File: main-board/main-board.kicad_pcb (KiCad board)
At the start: 2 copper layers, 101 x 101 mm, 18 parts, among them J1 C10418, J2 FH12-24S-0.5SH(55), U1 ESP-32s, U2 HT7333-A, U3 CH340E

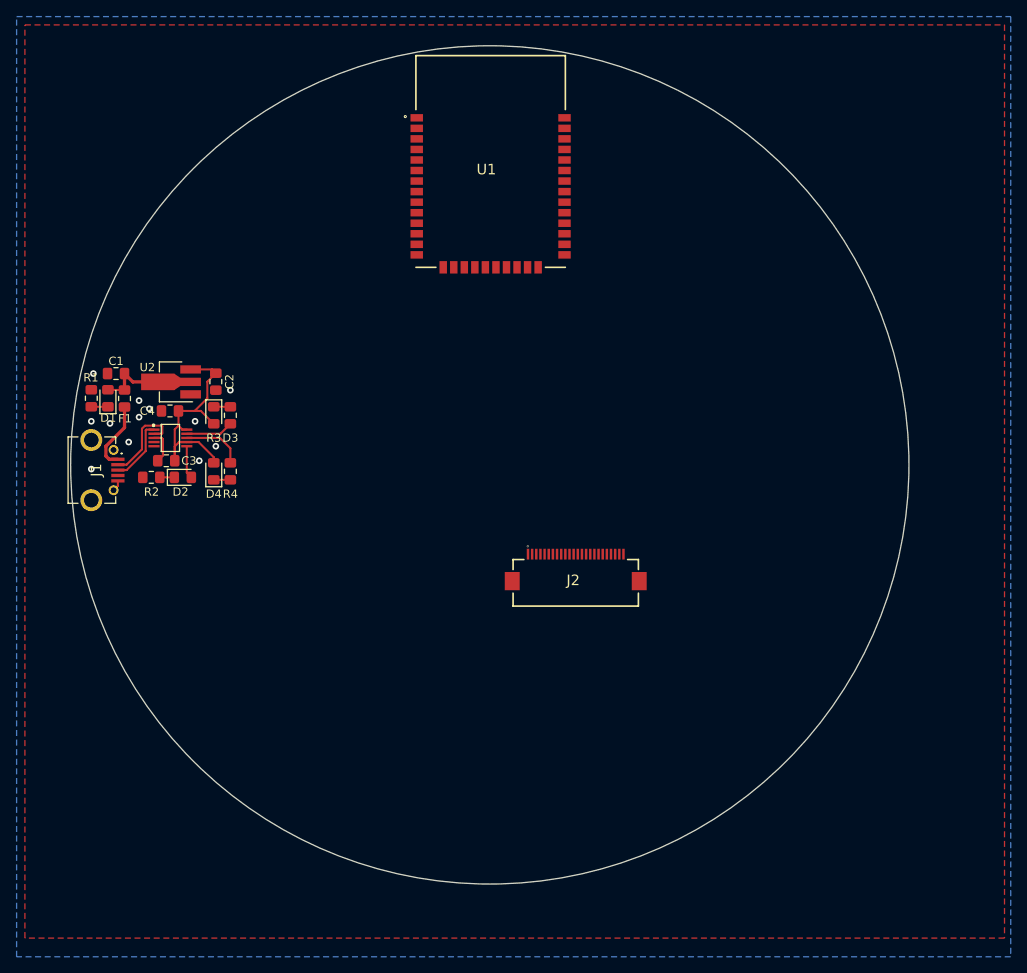
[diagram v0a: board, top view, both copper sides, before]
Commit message: battery holder
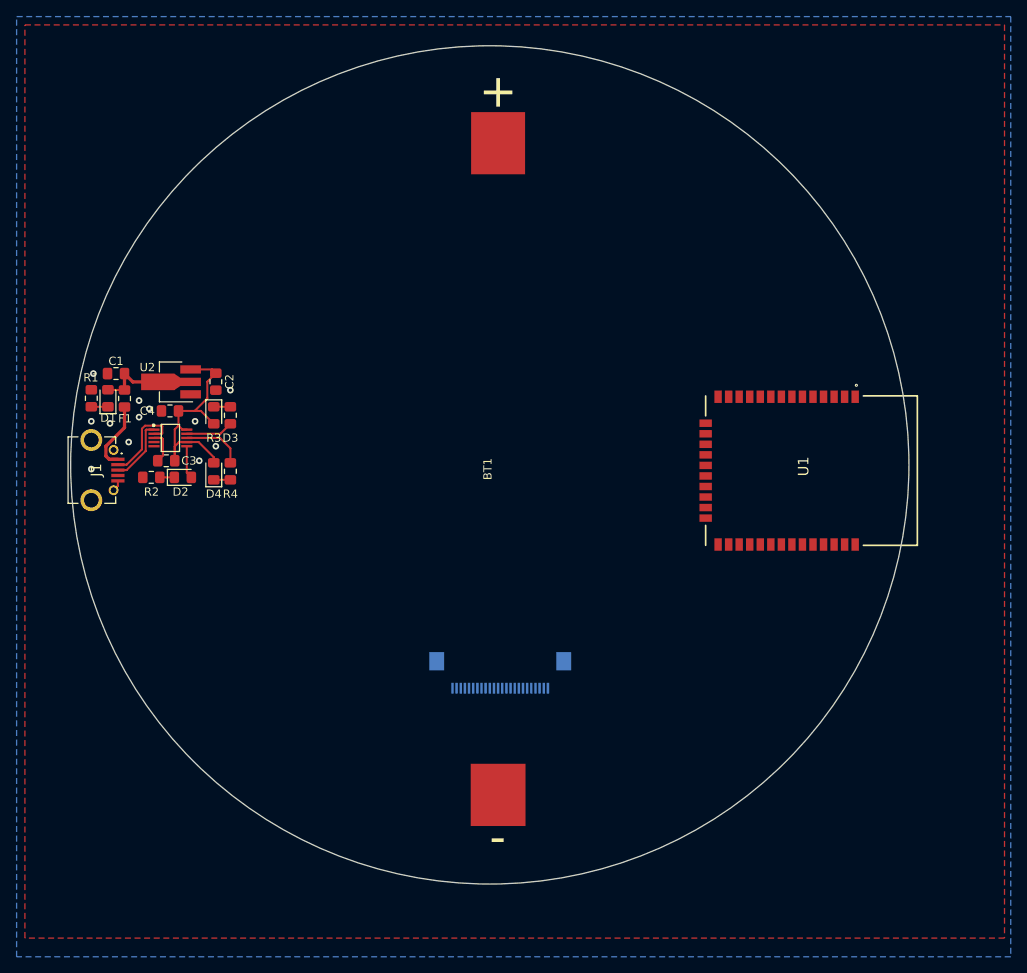
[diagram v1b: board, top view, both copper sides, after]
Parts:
- added BT1: Battery_Holder, water-lib:Battery Holder SMD, F.Cu at (146.0, 90.5)
- J2: moved to B.Cu
- moved U1 35.6 mm to (171.0, 90.7), turned to 270 degrees
- moved J2 17.4 mm to (146.2, 116.2)

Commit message: battery protection + buckboost
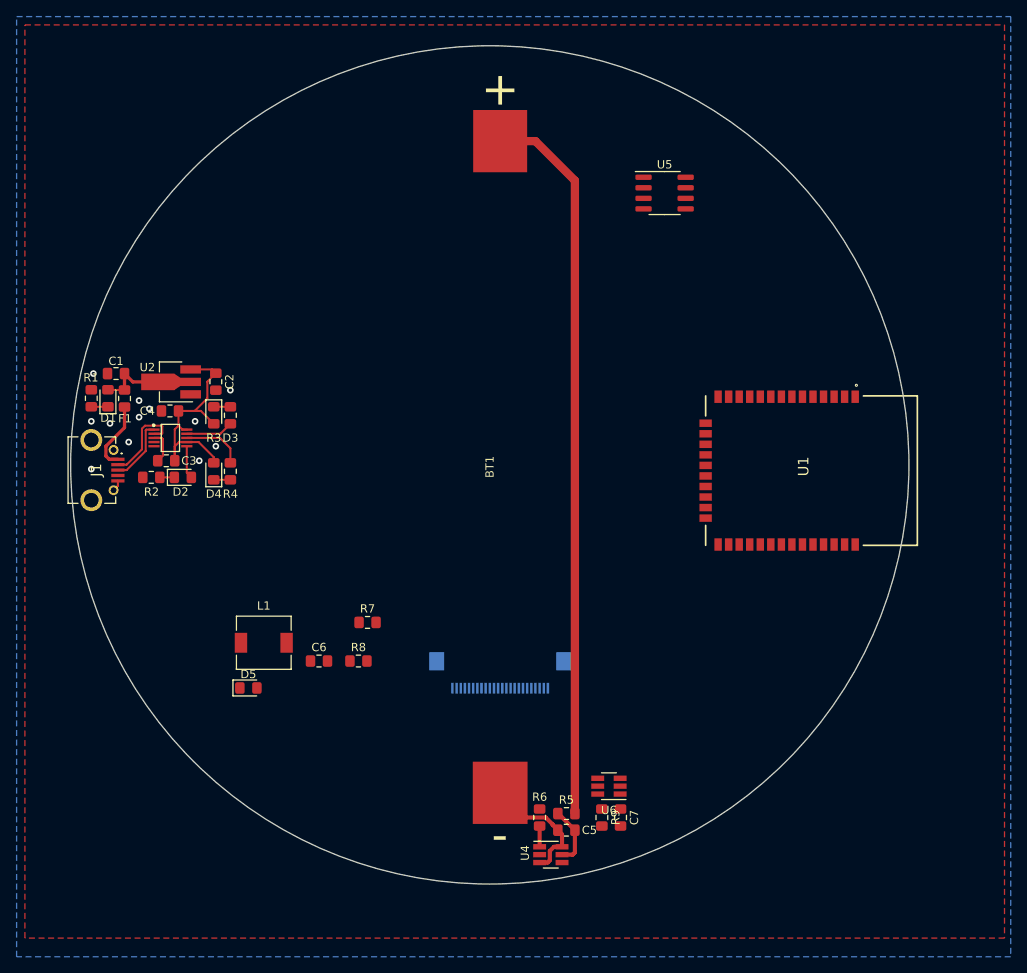
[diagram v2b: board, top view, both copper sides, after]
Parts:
- added C5: 0.1uF, Capacitor_SMD:C_0805_2012Metric_Pad1.15x1.40mm_HandSolder, F.Cu at (154.2, 134.0)
- added C6: 22uF, Capacitor_SMD:C_0805_2012Metric_Pad1.15x1.40mm_HandSolder, F.Cu at (124.4, 113.6)
- added C7: 22uF, Capacitor_SMD:C_0805_2012Metric_Pad1.15x1.40mm_HandSolder, F.Cu at (160.8, 132.5)
- added D5: D_Schottky, Diode_SMD:D_0805_2012Metric_Pad1.15x1.40mm_HandSolder, F.Cu at (115.9, 116.9)
- added L1: 22uH, Inductor_SMD:L_6.3x6.3_H3, F.Cu at (117.8, 111.4)
- added R5: 100, Resistor_SMD:R_0805_2012Metric_Pad1.15x1.40mm_HandSolder, F.Cu at (154.2, 132.0)
- added R6: 1k, Resistor_SMD:R_0805_2012Metric_Pad1.15x1.40mm_HandSolder, F.Cu at (151.0, 132.5)
- added R7: 10k, Resistor_SMD:R_0805_2012Metric_Pad1.15x1.40mm_HandSolder, F.Cu at (130.3, 109.0)
- added R8: 10k, Resistor_SMD:R_0805_2012Metric_Pad1.15x1.40mm_HandSolder, F.Cu at (129.2, 113.6)
- added R9: 10k, Resistor_SMD:R_0805_2012Metric_Pad1.15x1.40mm_HandSolder, F.Cu at (158.5, 132.5)
- added U4: DW06D, Package_TO_SOT_SMD:SOT-23-6_Handsoldering, F.Cu at (152.3, 136.9)
- added U5: IPS6404L-SQ-SPN, Package_SO:SOP-8_3.76x4.96mm_P1.27mm, F.Cu at (166.1, 57.3)
- added U6: SX1308, Package_TO_SOT_SMD:SOT-23-6_Handsoldering, F.Cu at (159.3, 128.7)
- BT1: footprint water-lib:Battery Holder SMD -> water-lib:Battery-Holder-SMD
- moved BT1 0.35 mm to (146.2, 90.2)
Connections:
- BT1 pad +: (no net) -> /VBAT
- BT1 pad -: (no net) -> Net-(BT1-Pad-)
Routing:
- net /VBAT: track 0.00 -> 87.2 mm
- net Net-(BT1-Pad-): track 0.00 -> 15.2 mm
- net Net-(C5-Pad1): track 0.00 -> 7.22 mm
- net Net-(R6-Pad2): track 0.00 -> 2.50 mm

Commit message: boost, LDOs, ribbon connerctions
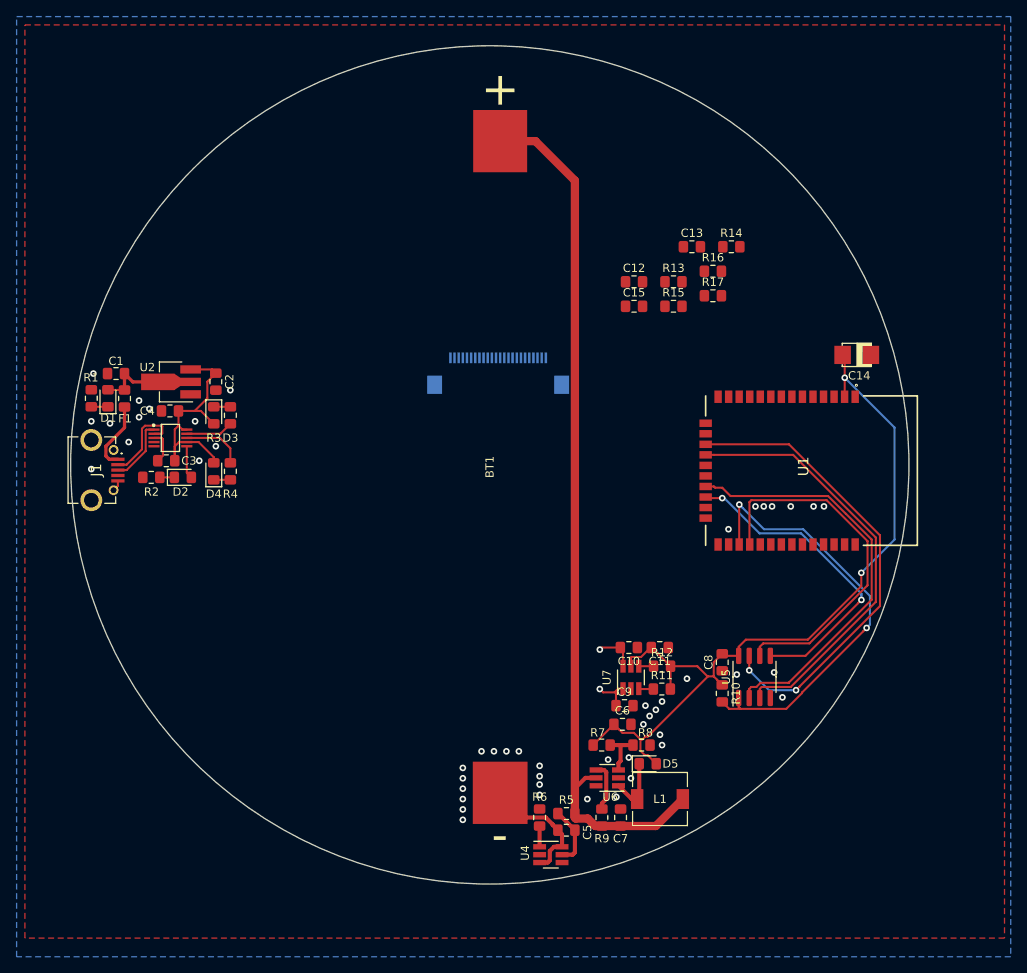
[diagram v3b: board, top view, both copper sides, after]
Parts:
- added C10: 1uF, Capacitor_SMD:C_0805_2012Metric_Pad1.15x1.40mm_HandSolder, F.Cu at (161.8, 112.0)
- added C11: 1uF, Capacitor_SMD:C_0805_2012Metric_Pad1.15x1.40mm_HandSolder, F.Cu at (165.5, 112.0)
- added C12: 15pF, Capacitor_SMD:C_0805_2012Metric_Pad1.15x1.40mm_HandSolder, F.Cu at (162.4, 67.9)
- added C13: 0.1uF, Capacitor_SMD:C_0805_2012Metric_Pad1.15x1.40mm_HandSolder, F.Cu at (169.3, 63.7)
- added C14: 100uF, water-lib:TAJB107M010RNJ, F.Cu at (189.2, 76.8)
- added C15: 1uF, Capacitor_SMD:C_0805_2012Metric_Pad1.15x1.40mm_HandSolder, F.Cu at (162.4, 70.9)
- added C8: 1uF, Capacitor_SMD:C_0805_2012Metric_Pad1.15x1.40mm_HandSolder, F.Cu at (173.0, 113.8)
- added C9: 1uF, Capacitor_SMD:C_0805_2012Metric_Pad1.15x1.40mm_HandSolder, F.Cu at (161.2, 119.0)
- added R10: 10k, Resistor_SMD:R_0805_2012Metric_Pad1.15x1.40mm_HandSolder, F.Cu at (173.0, 117.5)
- added R11: 10k, Resistor_SMD:R_0805_2012Metric_Pad1.15x1.40mm_HandSolder, F.Cu at (165.7, 117.0)
- added R12: 10k, Resistor_SMD:R_0805_2012Metric_Pad1.15x1.40mm_HandSolder, F.Cu at (165.8, 114.2)
- added R13: 1k, Resistor_SMD:R_0805_2012Metric_Pad1.15x1.40mm_HandSolder, F.Cu at (167.1, 67.9)
- added R14: 4k7, Resistor_SMD:R_0805_2012Metric_Pad1.15x1.40mm_HandSolder, F.Cu at (174.1, 63.7)
- added R15: 4k7, Resistor_SMD:R_0805_2012Metric_Pad1.15x1.40mm_HandSolder, F.Cu at (167.1, 70.9)
- added R16: 10k, Resistor_SMD:R_0805_2012Metric_Pad1.15x1.40mm_HandSolder, F.Cu at (171.9, 66.7)
- added R17: 4k7, Resistor_SMD:R_0805_2012Metric_Pad1.15x1.40mm_HandSolder, F.Cu at (171.9, 69.6)
- added U7: RT9011-CMGJ6, Package_TO_SOT_SMD:SOT-23-6_Handsoldering, F.Cu at (162.0, 115.6)
- R8: value 10k -> 2k2
- moved U5 59.3 mm to (176.9, 115.5), turned to 90 degrees
- moved L1 51.3 mm to (165.5, 130.2)
- moved D5 49.0 mm to (164.0, 126.0)
- moved J2 38.5 mm to (146.0, 77.8), turned to 180 degrees
- moved C6 37.3 mm to (161.0, 121.2)
- moved R8 35.6 mm to (163.3, 123.8)
- moved R7 31.8 mm to (158.5, 123.8)
- moved U6 1.02 mm to (159.2, 127.7)
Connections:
- net /VCC renamed /USB_PWR
- net Net-(J2-Pad18) renamed /CSI_VSYNC
- C2 pad 1: +3V3 -> VCC
- C3 pad 2: +3V3 -> VCC
- C4 pad 2: +3V3 -> VCC
- D3 pad 2: +3V3 -> VCC
- D4 pad 2: +3V3 -> VCC
- J2 pad 10: Net-(J2-Pad10) -> GND
- J2 pad 11: Net-(J2-Pad11) -> /CSI_D6
- J2 pad 12: Net-(J2-Pad12) -> /CSI_MCLK
- J2 pad 13: Net-(J2-Pad13) -> /CSI_D7
- J2 pad 14: Net-(J2-Pad14) -> +3V3
- J2 pad 15: Net-(J2-Pad15) -> +1V2
- J2 pad 16: Net-(J2-Pad16) -> /CSI_HSYNC
- J2 pad 19: Net-(J2-Pad19) -> /CAM_RST
- J2 pad 20: Net-(J2-Pad20) -> /TWI_SCK
- J2 pad 21: Net-(J2-Pad21) -> +2V8
- J2 pad 22: Net-(J2-Pad22) -> /TWI_SDA
- J2 pad 23: Net-(J2-Pad23) -> GND
- J2 pad 25: (no net) -> GND
- J2 pad 26: (no net) -> Net-(J2-Pad26)
- J2 pad 3: Net-(J2-Pad3) -> /CSI_D2
- J2 pad 4: Net-(J2-Pad4) -> /CSI_D1
- J2 pad 5: Net-(J2-Pad5) -> /CSI_D3
- J2 pad 6: Net-(J2-Pad6) -> /CSI_D0
- J2 pad 7: Net-(J2-Pad7) -> /CSI_D4
- J2 pad 8: Net-(J2-Pad8) -> /CSI_PCLK
- J2 pad 9: Net-(J2-Pad9) -> /CSI_D5
- U1 pad 1: Net-(U1-Pad1) -> GND
- U1 pad 11: Net-(U1-Pad11) -> /TWI_SDA
- U1 pad 12: Net-(U1-Pad12) -> /TWI_SCK
- U1 pad 17: Net-(U1-Pad17) -> /SD2
- U1 pad 18: Net-(U1-Pad18) -> /SD3
- U1 pad 2: Net-(U1-Pad2) -> +3V3
- U1 pad 21: Net-(U1-Pad21) -> /SD0
- U1 pad 22: Net-(U1-Pad22) -> /SD1
- U1 pad 26: Net-(U1-Pad26) -> /CSI_MCLK
- U1 pad 27: Net-(U1-Pad27) -> /IO16
- U1 pad 28: Net-(U1-Pad28) -> /PSRAM_CLK
- U1 pad 29: Net-(U1-Pad29) -> /CSI_D0
- U1 pad 30: Net-(U1-Pad30) -> /CSI_D1
- U1 pad 31: Net-(U1-Pad31) -> /CSI_D2
- U1 pad 33: Net-(U1-Pad33) -> /CSI_D3
- U1 pad 36: Net-(U1-Pad36) -> /CSI_PCLK
- U1 pad 37: Net-(U1-Pad37) -> /CSI_HSYNC
- U1 pad 4: Net-(U1-Pad4) -> /CSI_D4
- U1 pad 5: Net-(U1-Pad5) -> /CSI_D5
- U1 pad 6: Net-(U1-Pad6) -> /CSI_D6
- U1 pad 7: Net-(U1-Pad7) -> /CSI_D7
- U2 pad 3: +3V3 -> VCC
- U3 pad 10: +3V3 -> VCC
- U3 pad 7: +3V3 -> VCC
- U5 pad 1: Net-(U5-Pad1) -> /IO16
- U5 pad 2: Net-(U5-Pad2) -> /SD0
- U5 pad 3: Net-(U5-Pad3) -> /SD3
- U5 pad 4: Net-(U5-Pad4) -> GND
- U5 pad 5: Net-(U5-Pad5) -> /SD1
- U5 pad 6: Net-(U5-Pad6) -> /PSRAM_CLK
- U5 pad 7: Net-(U5-Pad7) -> /SD2
- U5 pad 8: Net-(U5-Pad8) -> +3V3
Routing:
- net +3V3: track 29.2 -> 98.4 mm, vias 0 -> 2
- net /SD2: track 0.00 -> 56.8 mm, vias 0 -> 2
- net /IO16: track 0.00 -> 52.4 mm, vias 0 -> 2
- net /SD3: track 0.00 -> 52.0 mm
- net /SD0: track 0.00 -> 50.2 mm
- net /PSRAM_CLK: track 0.00 -> 43.9 mm
- net /SD1: track 0.00 -> 38.1 mm, vias 0 -> 2
- net VCC: track 0.00 -> 29.2 mm
- net /VBAT: track 87.2 -> 108.6 mm
- net Net-(D5-Pad1): track 0.00 -> 7.27 mm
- net Net-(R9-Pad1): track 0.00 -> 5.99 mm
- net Net-(R7-Pad2): track 0.00 -> 5.85 mm
- net +1V2: track 0.00 -> 4.96 mm, vias 0 -> 1
- net +2V8: track 0.00 -> 4.93 mm, vias 0 -> 1
- net Net-(R12-Pad1): track 0.00 -> 1.78 mm
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
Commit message: ribbon connections and reset sw
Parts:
- added R18: 10k, Resistor_SMD:R_0805_2012Metric_Pad1.15x1.40mm_HandSolder, F.Cu at (185.2, 73.8)
- added SW1: RESET, Button_Switch_SMD:SW_SPST_CK_RS282G05A3, F.Cu at (185.1, 70.4)
- moved R17 39.6 mm to (132.5, 74.1)
- moved C13 37.8 mm to (132.5, 72.2)
- moved R13 36.7 mm to (132.4, 79.8), turned to 180 degrees
- moved R16 36.3 mm to (174.0, 102.9), turned to 270 degrees
- moved C12 31.5 mm to (132.5, 77.9)
- moved C15 30.3 mm to (132.5, 76.0)
- moved R14 15.4 mm to (159.1, 67.4)
- moved R15 9.65 mm to (159.1, 65.5)
- moved D5 0.21 mm to (164.0, 125.8)
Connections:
- net Net-(J2-Pad17) renamed /CSI_PWD
- U1 pad 10: Net-(U1-Pad10) -> /CSI_VSYNC
- U1 pad 3: Net-(U1-Pad3) -> /EN
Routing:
- net +3V3: track 98.4 -> 186.8 mm, vias 2 -> 4
- net /CSI_PCLK: track 0.00 -> 72.5 mm, vias 1 -> 2
- net /CSI_HSYNC: track 0.00 -> 61.4 mm
- net /TWI_SCK: track 0.00 -> 55.2 mm, vias 0 -> 1
- net /CSI_D3: track 0.00 -> 51.2 mm
- net /TWI_SDA: track 0.00 -> 51.1 mm, vias 0 -> 1
- net +2V8: track 4.93 -> 54.4 mm, vias 1 -> 3
- net +1V2: track 4.96 -> 53.5 mm, vias 1 -> 3
- net /CSI_D6: track 0.00 -> 45.7 mm, vias 0 -> 1
- net /CSI_D0: track 0.00 -> 45.5 mm, vias 0 -> 1
- net /CSI_VSYNC: track 0.00 -> 45.4 mm, vias 0 -> 1
- net /CSI_D2: track 0.00 -> 45.3 mm
- net /CSI_D7: track 0.00 -> 45.1 mm, vias 0 -> 1
- net /CSI_D5: track 0.00 -> 44.9 mm, vias 0 -> 1
- net /CSI_D4: track 0.00 -> 44.9 mm, vias 0 -> 1
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
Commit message: SD card
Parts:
- added J3: TF-01A, water-lib:TF-01A, F.Cu at (125.3, 54.6)
- added Q1: Q_NPN_BCE, Package_TO_SOT_SMD:SOT-23, F.Cu at (108.5, 97.9)
- added Q2: Q_NPN_BCE, Package_TO_SOT_SMD:SOT-23, F.Cu at (108.5, 94.3)
- added R19: 10k, Resistor_SMD:R_0805_2012Metric_Pad1.15x1.40mm_HandSolder, F.Cu at (105.7, 96.5)
- added R20: 10k, Resistor_SMD:R_0805_2012Metric_Pad1.15x1.40mm_HandSolder, F.Cu at (104.6, 93.3)
- added U8: SN74LVC125ADBR, Package_SO:TSSOP-14_4.4x5mm_P0.65mm, F.Cu at (111.1, 61.5)
- SW1: value RESET -> SW_DIP_x01
- moved R2 0.36 mm to (104.6, 91.4)
- moved D2 0.35 mm to (108.4, 91.5)
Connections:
- U1 pad 25: Net-(U1-Pad25) -> /IO0
- U1 pad 34: Net-(U1-Pad34) -> /TX
- U1 pad 35: Net-(U1-Pad35) -> /RX
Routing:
- net /EN: track 14.1 -> 128.8 mm, vias 2 -> 6
- net /TX: track 7.52 -> 96.6 mm, vias 0 -> 2
- net /RX: track 5.75 -> 93.0 mm, vias 0 -> 2
- net /IO0: track 0.00 -> 78.9 mm, vias 0 -> 2
- net /CTS: track 0.00 -> 16.4 mm
- net /RTS: track 0.00 -> 14.4 mm
- net Net-(Q1-Pad1): track 0.00 -> 4.36 mm
- net GND: track 8.64 -> 12.6 mm, vias 53 -> 57
- net Net-(Q2-Pad1): track 0.00 -> 1.83 mm
- net /CSI_D3: track 51.2 -> 50.2 mm
- net /D-: track 10.6 -> 11.4 mm
- net /D+: track 7.83 -> 8.46 mm
